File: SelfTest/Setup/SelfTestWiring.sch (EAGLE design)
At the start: 13 parts

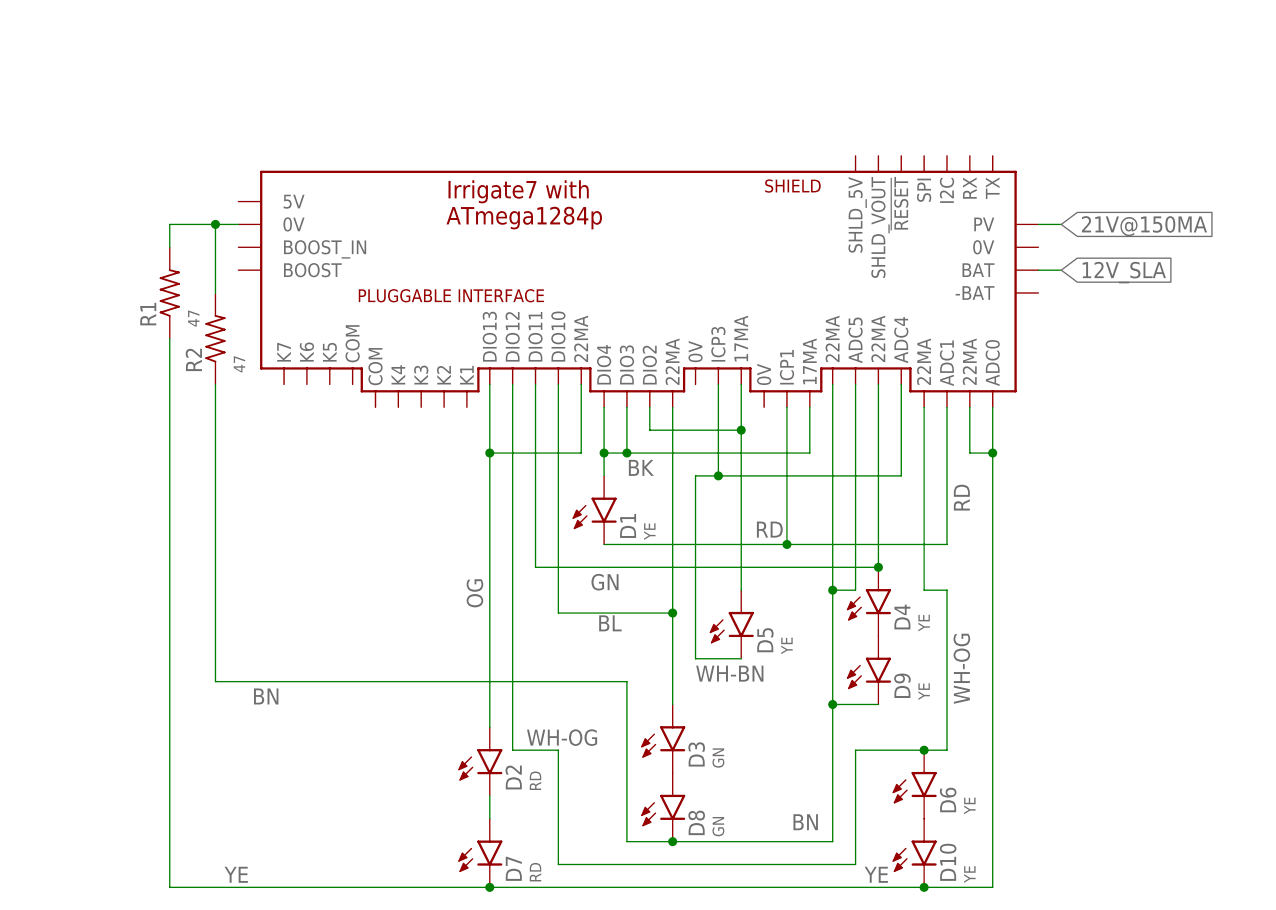
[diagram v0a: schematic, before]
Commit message: Solenoid: port from RPUno, this is also used for testing
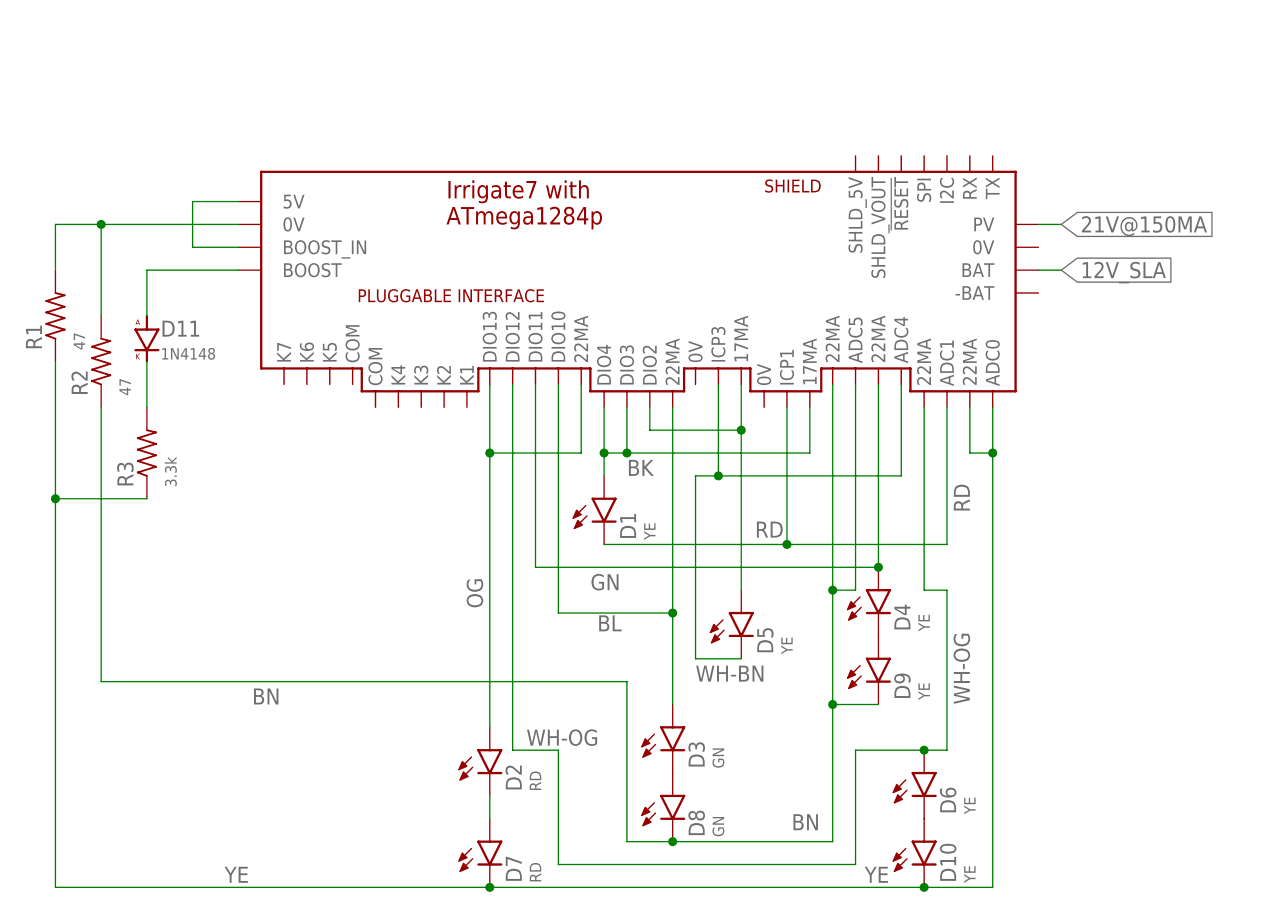
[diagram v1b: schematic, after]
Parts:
- added D11: 1N4148, D-GP:DDO41-10
- added R3: 3.3k, R-C:R0805
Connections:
- new net N$1: U$1.5V, U$1.BOOST_IN
- new net N$2: D11.A, U$1.BOOST
- new net N$3: D11.K, R3.2
- net YE: now also R3.1
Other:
- note added: "BOOST OUTPUT IS SET WITH A JUMPER AT 9V R1 HAS 2.7mA AT 12V R1 HAS 3.6mA AT 24V R1 HAS 7.2mA DIO13 LOW, OTHER CURR SOURCES ARE OFF"
- moved on the sheet: R1, R2
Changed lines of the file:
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@@
 <part name="D9" library="D-LED" deviceset="LED" device="5MM" value="YE"/>
 <part name="D4" library="D-LED" deviceset="LED" device="5MM" value="YE"/>
+<part name="D11" library="D-GP" deviceset="D" device="DO41-10" value="1N4148"/>
+<part name="R3" library="R-C" deviceset="R" device="0805" value="3.3k"/>
 </parts>
 <sheets>
@@
 <plain>
 <text x="-40.64" y="124.46" size="5.08" layer="98">SELF TEST</text>
+<text x="-97.028" y="65.278" size="1.778" layer="98">BOOST OUTPUT IS SET
+WITH A JUMPER
+AT 9V R1 HAS 2.7mA
+AT 12V R1 HAS 3.6mA
+AT 24V R1 HAS 7.2mA
+DIO13 LOW, OTHER CURR
+SOURCES ARE OFF</text>
 </plain>
 <instances>
@@
 <instance part="D1" gate="G$1" x="-43.18" y="83.82"/>
 <instance part="D10" gate="G$1" x="-7.62" y="45.72"/>
-<instance part="R1" gate="G$1" x="-91.44" y="106.68" rot="R90"/>
+<instance part="R1" gate="G$1" x="-104.14" y="104.14" rot="R90"/>
 <instance part="D2" gate="G$1" x="-55.88" y="55.88"/>
-<instance part="R2" gate="G$1" x="-86.36" y="101.6" rot="R90"/>
+<instance part="R2" gate="G$1" x="-99.06" y="99.06" rot="R90"/>
 <instance part="D5" gate="G$1" x="-27.94" y="71.12"/>
 <instance part="D8" gate="G$1" x="-35.56" y="50.8"/>
@@
 <instance part="D9" gate="G$1" x="-12.7" y="66.04"/>
 <instance part="D4" gate="G$1" x="-12.7" y="73.66"/>
+<instance part="D11" gate="G$1" x="-93.98" y="101.6"/>
+<instance part="R3" gate="G$1" x="-93.98" y="88.9" rot="R90"/>
 </instances>
 <busses>
@@
 <label x="-85.344" y="41.148" size="1.778" layer="91"/>
 <label x="-14.224" y="41.148" size="1.778" layer="91"/>
-<wire x1="-91.44" y1="101.6" x2="-91.44" y2="40.64" width="0.1524" layer="91"/>
-<wire x1="-91.44" y1="40.64" x2="-55.88" y2="40.64" width="0.1524" layer="91"/>
+<wire x1="-104.14" y1="99.06" x2="-104.14" y2="83.82" width="0.1524" layer="91"/>
+<wire x1="-104.14" y1="83.82" x2="-104.14" y2="40.64" width="0.1524" layer="91"/>
+<wire x1="-104.14" y1="40.64" x2="-55.88" y2="40.64" width="0.1524" layer="91"/>
 <junction x="-55.88" y="40.64"/>
+<pinref part="R3" gate="G$1" pin="1"/>
+<wire x1="-93.98" y1="83.82" x2="-104.14" y2="83.82" width="0.1524" layer="91"/>
+<junction x="-104.14" y="83.82"/>
 </segment>
 </net>
@@
 <segment>
 <pinref part="R1" gate="G$1" pin="2"/>
-<wire x1="-91.44" y1="111.76" x2="-91.44" y2="114.3" width="0.1524" layer="91"/>
-<wire x1="-91.44" y1="114.3" x2="-86.36" y2="114.3" width="0.1524" layer="91"/>
+<wire x1="-104.14" y1="109.22" x2="-104.14" y2="114.3" width="0.1524" layer="91"/>
+<wire x1="-104.14" y1="114.3" x2="-99.06" y2="114.3" width="0.1524" layer="91"/>
 <pinref part="U$1" gate="G$1" pin="0V"/>
-<wire x1="-86.36" y1="114.3" x2="-83.82" y2="114.3" width="0.1524" layer="91"/>
-<wire x1="-86.36" y1="114.3" x2="-86.36" y2="106.68" width="0.1524" layer="91"/>
-<junction x="-86.36" y="114.3"/>
+<wire x1="-99.06" y1="114.3" x2="-83.82" y2="114.3" width="0.1524" layer="91"/>
+<wire x1="-99.06" y1="114.3" x2="-99.06" y2="104.14" width="0.1524" layer="91"/>
+<junction x="-99.06" y="114.3"/>
 <pinref part="R2" gate="G$1" pin="2"/>
 </segment>
@@
 <junction x="-35.56" y="45.72"/>
 <wire x1="-40.64" y1="45.72" x2="-40.64" y2="63.5" width="0.1524" layer="91"/>
-<wire x1="-40.64" y1="63.5" x2="-86.36" y2="63.5" width="0.1524" layer="91"/>
-<wire x1="-86.36" y1="63.5" x2="-86.36" y2="96.52" width="0.1524" layer="91"/>
+<wire x1="-40.64" y1="63.5" x2="-99.06" y2="63.5" width="0.1524" layer="91"/>
+<wire x1="-99.06" y1="63.5" x2="-99.06" y2="93.98" width="0.1524" layer="91"/>
 </segment>
 </net>
@@
 </segment>
 </net>
+<net name="N$1" class="0">
+<segment>
+<pinref part="U$1" gate="G$1" pin="5V"/>
+<wire x1="-83.82" y1="116.84" x2="-88.9" y2="116.84" width="0.1524" layer="91"/>
+<wire x1="-88.9" y1="116.84" x2="-88.9" y2="111.76" width="0.1524" layer="91"/>
+<pinref part="U$1" gate="G$1" pin="BOOST_IN"/>
+<wire x1="-88.9" y1="111.76" x2="-83.82" y2="111.76" width="0.1524" layer="91"/>
+</segment>
+</net>
+<net name="N$2" class="0">
+<segment>
+<pinref part="U$1" gate="G$1" pin="BOOST"/>
+<wire x1="-83.82" y1="109.22" x2="-93.98" y2="109.22" width="0.1524" layer="91"/>
+<pinref part="D11" gate="G$1" pin="A"/>
+<wire x1="-93.98" y1="109.22" x2="-93.98" y2="104.14" width="0.1524" layer="91"/>
+</segment>
+</net>
+<net name="N$3" class="0">
+<segment>
+<pinref part="D11" gate="G$1" pin="K"/>
+<pinref part="R3" gate="G$1" pin="2"/>
+<wire x1="-93.98" y1="99.06" x2="-93.98" y2="93.98" width="0.1524" layer="91"/>
+</segment>
+</net>

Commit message: BlinkLED: updates for ^5
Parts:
- removed D10, D5, D6, D9: YE, D-LED:LED5MM
- removed D11: 1N4148, D-GP:DDO41-10
- removed D7: RD, D-LED:LED5MM
- removed D8: GN, D-LED:LED5MM
- removed U$1: IRRIGATE7, Documentation:IRRIGATE7
- added C1: PW1J222, C-Al:C-AL7.5X18
- added R4, R5, R6, R7, R8: 100, R-C:R0805
- added U$2: IRRIGATE7, Documentation:IRRIGATE7
- D1: value YE -> GN
- D2: value RD -> YE
- D3: value GN -> RD
- R1: value 47 -> 100||100||100
- R2: value 47 -> 100
- R3: value 3.3k -> 100
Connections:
- removed net 12V_SLA: U$1.BAT
- removed net 21V@150MA: U$1.PV
- removed net BK: D1.A, U$1.17MA@ICP1, U$1.DIO3, U$1.DIO4
- removed net BN: D8.K, D9.K, R2.1, U$1.22MA@ADC5, U$1.ADC5
- removed net N$14: D10.A, D6.K
- removed net N$15: D3.K, D8.A
- removed net N$18: D4.K, D9.A
- removed net RD: D1.K, U$1.ADC1, U$1.ICP1
- removed net WH-BN: D5.K, U$1.ADC4, U$1.ICP3
- removed net WH-OG: D6.A, U$1.22MA@ADC1, U$1.DIO12
- removed net YE: D10.K, D7.K, R1.1, R3.1, U$1.22MA@ADC0, U$1.ADC0
- new net 12V8@200MA: U$2.PWR
- new net GY: D4.A, U$2.ADC3, U$2.CS2_22MA, U$2.TX1
- new net N$10: C1.-, U$2.0V
- new net N$12: R7.2, U$2.K6
- new net N$5: R5.2, U$2.K4
- new net N$6: R4.2, U$2.K3
- new net N$7: R3.2, U$2.K2
- new net N$8: R6.2, U$2.K5
- new net N$9: R6.1, R7.1, R8.1, U$2.COM@K5
- new net VT: D2.K, D3.K, D4.K, R1.1, U$2.22MA@IO, U$2.ADC0, U$2.CS1_22MA
- new net WH: D2.A, U$2.CS3_22MA, U$2.RX1
- net BL: now also D1.A, U$2.ADC2, U$2.CS_ICP1_17MA; no longer D3.A, U$1.22MA@DIO2, U$1.DIO10
- net GN: now also D3.A, U$2.CS0_22MA; no longer D4.A, U$1.22MA@ADC4, U$1.DIO11
- net N$1: now also U$2.5V, U$2.BOOST_IN; no longer U$1.5V, U$1.BOOST_IN
- net N$11: now also C1.+, U$2.BOOST; no longer D5.A, U$1.17MA@ICP3, U$1.DIO2
- net N$13: now also R8.2, U$2.K7; no longer D2.K, D7.A
- net N$2: now also R2.2, U$2.K1; no longer D11.A, U$1.BOOST
- net N$3: now also R2.1, R3.1, R4.1, R5.1, U$2.COM@K4; no longer D11.K, R3.2
- net N$4: now also U$2.0V@ADC0; no longer R2.2, U$1.0V
- net OG: now also D1.K, U$2.ADC1, U$2.ICP1; no longer D2.A, U$1.22MA@DIO10, U$1.DIO13
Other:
- note added: "240mA@24V IS 5.76W PULSE 50mSec"
- note added: "C1 2200uF 63V 3.2A RPPL 18ODx40H mm"
- note removed: "BOOST OUTPUT IS SET WITH A JUMPER AT 9V R1 HAS 2.7mA AT 12V R1 HAS 3.6mA AT 24V R1 HAS 7.2mA DIO13 LOW, OTHER CURR SOURCES ARE OFF"
- moved on the sheet: D1, D2, D3, D4, R1, R2, R3
